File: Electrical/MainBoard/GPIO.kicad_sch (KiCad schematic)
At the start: 1 part, among them J17 GPIO

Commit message: Begin layout of pcb
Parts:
- renumbered J17 to J16
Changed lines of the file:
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@@
   (symbol (lib_id "Connector_Generic:Conn_02x10_Odd_Even") (at 149.86 94.615 0) (unit 1)
     (in_bom yes) (on_board yes) (dnp no) (fields_autoplaced)
-    (property "Reference" "J17" (at 151.13 78.74 0)
+    (property "Reference" "J16" (at 151.13 78.74 0)
       (effects (font (size 1.27 1.27)))
     )
@@
       (project "MainBoard"
         (path "/bd24c4db-4e36-4117-bd4f-5228ef241da9/7681952e-9ac4-4545-8f8a-d83e518f0640"
-          (reference "J17") (unit 1)
+          (reference "J16") (unit 1)
         )
       )

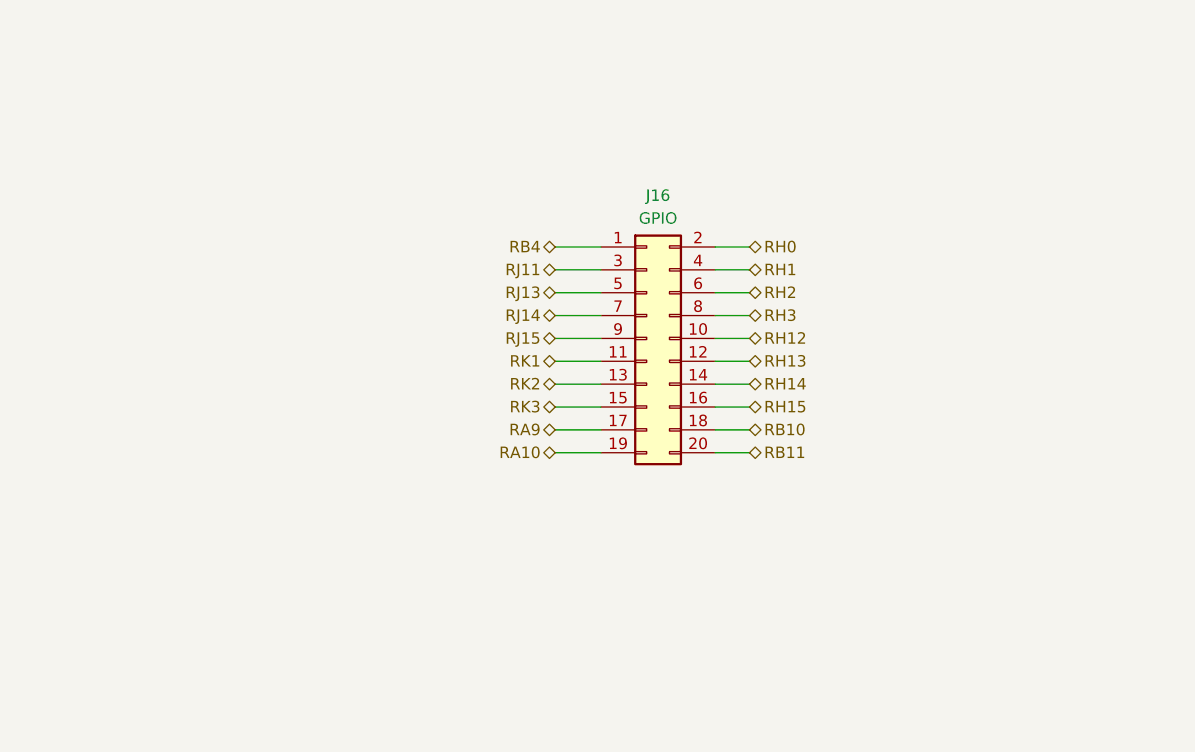
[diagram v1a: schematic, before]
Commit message: First Pass at the routing
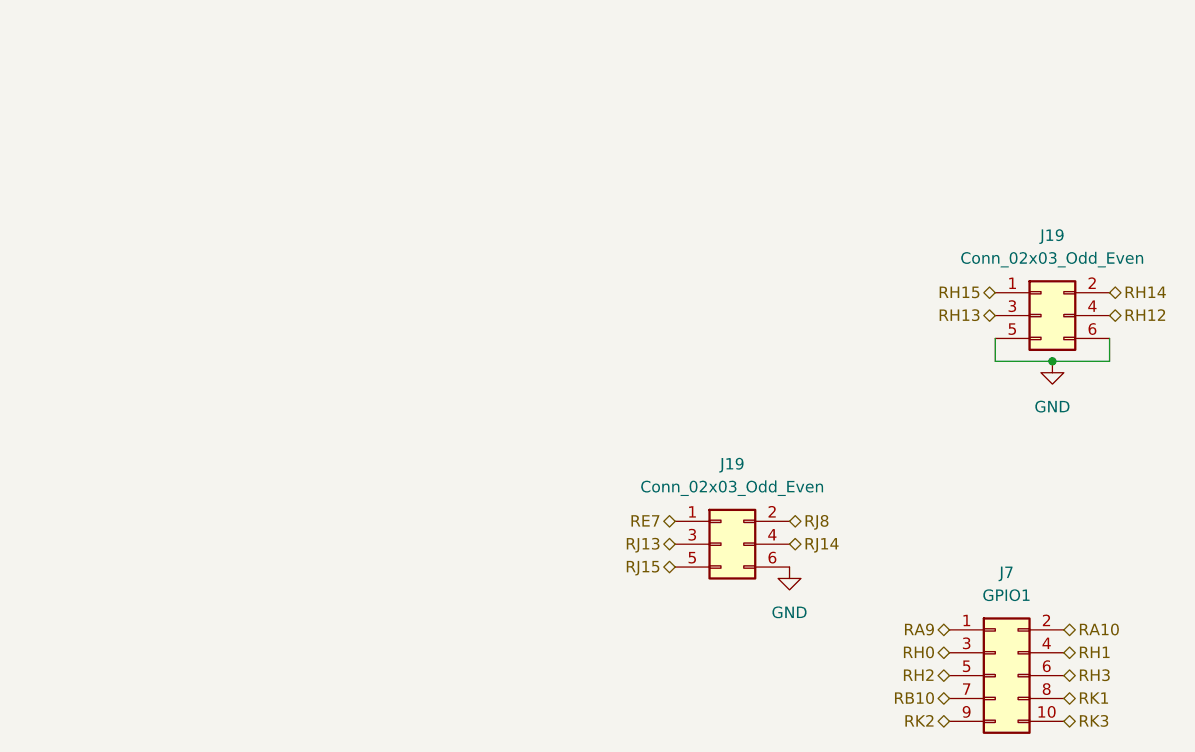
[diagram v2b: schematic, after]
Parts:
- removed J16: GPIO, Connector_PinHeader_2.54mm:PinHeader_2x10_P2.54mm_Vertical, symbol Connector_Generic:Conn_02x10_Odd_Even
- added J19 (x2): Conn_02x03_Odd_Even, Connector_PinHeader_2.54mm:PinHeader_2x03_P2.54mm_Vertical, symbol Connector_Generic:Conn_02x03_Odd_Even
- added J7: GPIO1, Connector_PinHeader_2.54mm:PinHeader_2x05_P2.54mm_Vertical, symbol Connector_Generic:Conn_02x05_Odd_Even
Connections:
- net RA10: now also J7.2 (Pin_2)
- net RA9: now also J7.1 (Pin_1)
- net RB10: now also J7.7 (Pin_7)
- net RH0: now also J7.3 (Pin_3)
- net RH1: now also J7.4 (Pin_4)
- net RH12: now also J19.4 (Pin_4)
- net RH13: now also J19.3 (Pin_3)
- net RH14: now also J19.2 (Pin_2)
- net RH15: now also J19.1 (Pin_1)
- net RH2: now also J7.5 (Pin_5)
- net RH3: now also J7.6 (Pin_6)
- net RJ13: now also J19.3 (Pin_3)
- net RJ14: now also J19.4 (Pin_4)
- net RJ15: now also J19.5 (Pin_5)
- net RK1: now also J7.8 (Pin_8)
- net RK2: now also J7.9 (Pin_9)
- net RK3: now also J7.10 (Pin_10)
- new net GND: J19.5 (Pin_5), J19.6 (Pin_6), J19.6 (Pin_6)
- new net RE7: J19.1 (Pin_1)
- new net RJ8: J19.2 (Pin_2)

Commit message: Add some finishing touches and create preliminary boms
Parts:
- J19: Mfr (none) -> Amphenol ICC (FCI); Mfr P/N (none) -> 10129381-906002BLF; Supplier 1 (none) -> DigiKey; Supplier 1 P/N (none) -> 10129381-906002BLF-ND
- J7: Mfr (none) -> Amphenol ICC (FCI); Mfr P/N (none) -> 10129381-910001BLF; Supplier 1 (none) -> DigiKey; Supplier 1 P/N (none) -> 10129381-910001BLF-ND
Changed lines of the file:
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@@
       (effects (font (size 1.27 1.27)) hide)
     )
-    (property "Datasheet" "~" (at 193.675 92.075 0)
+    (property "Datasheet" "https://cdn.amphenol-cs.com/media/wysiwyg/files/drawing/10129381.pdf" (at 193.675 92.075 0)
       (effects (font (size 1.27 1.27)) hide)
     )
-    (property "Description" "" (at 193.675 92.075 0)
+    (property "Description" "CONN HEADER VERT 6POS 2.54MM" (at 193.675 92.075 0)
       (effects (font (size 1.27 1.27)) hide)
     )
-    (property "Mfr" "" (at 193.675 92.075 0)
+    (property "Mfr" "Amphenol ICC (FCI)" (at 193.675 92.075 0)
       (effects (font (size 1.27 1.27)) hide)
     )
-    (property "Mfr P/N" "" (at 193.675 92.075 0)
+    (property "Mfr P/N" "10129381-906002BLF" (at 193.675 92.075 0)
       (effects (font (size 1.27 1.27)) hide)
     )
-    (property "Supplier 1" "" (at 193.675 92.075 0)
+    (property "Supplier 1" "DigiKey" (at 193.675 92.075 0)
       (effects (font (size 1.27 1.27)) hide)
     )
-    (property "Supplier 1 P/N" "" (at 193.675 92.075 0)
+    (property "Supplier 1 P/N" "10129381-906002BLF-ND" (at 193.675 92.075 0)
       (effects (font (size 1.27 1.27)) hide)
     )
@@
       (effects (font (size 1.27 1.27)) hide)
     )
-    (property "Datasheet" "~" (at 188.595 132.08 0)
+    (property "Datasheet" "https://cdn.amphenol-cs.com/media/wysiwyg/files/drawing/10129381.pdf" (at 188.595 132.08 0)
       (effects (font (size 1.27 1.27)) hide)
     )
-    (property "Description" "" (at 188.595 132.08 0)
+    (property "Description" "CONN HEADER VERT 10POS 2.54MM" (at 188.595 132.08 0)
       (effects (font (size 1.27 1.27)) hide)
     )
-    (property "Mfr" "" (at 188.595 132.08 0)
+    (property "Mfr" "Amphenol ICC (FCI)" (at 188.595 132.08 0)
       (effects (font (size 1.27 1.27)) hide)
     )
-    (property "Mfr P/N" "" (at 188.595 132.08 0)
+    (property "Mfr P/N" "10129381-910001BLF" (at 188.595 132.08 0)
       (effects (font (size 1.27 1.27)) hide)
     )
-    (property "Supplier 1" "" (at 188.595 132.08 0)
+    (property "Supplier 1" "DigiKey" (at 188.595 132.08 0)
       (effects (font (size 1.27 1.27)) hide)
     )
-    (property "Supplier 1 P/N" "" (at 188.595 132.08 0)
+    (property "Supplier 1 P/N" "10129381-910001BLF-ND" (at 188.595 132.08 0)
       (effects (font (size 1.27 1.27)) hide)
     )
@@
       (effects (font (size 1.27 1.27)) hide)
     )
-    (property "Datasheet" "~" (at 158.115 117.475 0)
+    (property "Datasheet" "https://cdn.amphenol-cs.com/media/wysiwyg/files/drawing/10129381.pdf" (at 158.115 117.475 0)
       (effects (font (size 1.27 1.27)) hide)
     )
-    (property "Description" "" (at 158.115 117.475 0)
+    (property "Description" "CONN HEADER VERT 6POS 2.54MM" (at 158.115 117.475 0)
       (effects (font (size 1.27 1.27)) hide)
     )
-    (property "Mfr" "" (at 158.115 117.475 0)
+    (property "Mfr" "Amphenol ICC (FCI)" (at 158.115 117.475 0)
       (effects (font (size 1.27 1.27)) hide)
     )
-    (property "Mfr P/N" "" (at 158.115 117.475 0)
+    (property "Mfr P/N" "10129381-906002BLF" (at 158.115 117.475 0)
       (effects (font (size 1.27 1.27)) hide)
     )
-    (property "Supplier 1" "" (at 158.115 117.475 0)
+    (property "Supplier 1" "DigiKey" (at 158.115 117.475 0)
       (effects (font (size 1.27 1.27)) hide)
     )
-    (property "Supplier 1 P/N" "" (at 158.115 117.475 0)
+    (property "Supplier 1 P/N" "10129381-906002BLF-ND" (at 158.115 117.475 0)
       (effects (font (size 1.27 1.27)) hide)
     )

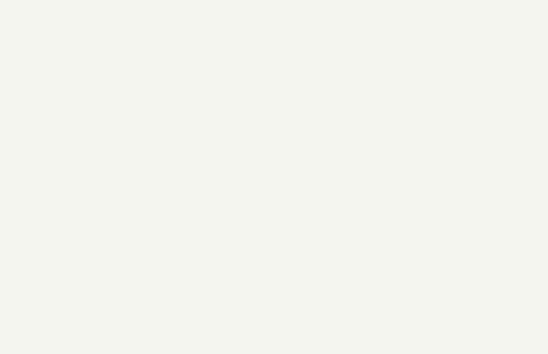
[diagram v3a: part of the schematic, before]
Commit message: Finish final board design for Rev 0.1 Main board and reflective Sensor. Created Gerbers.
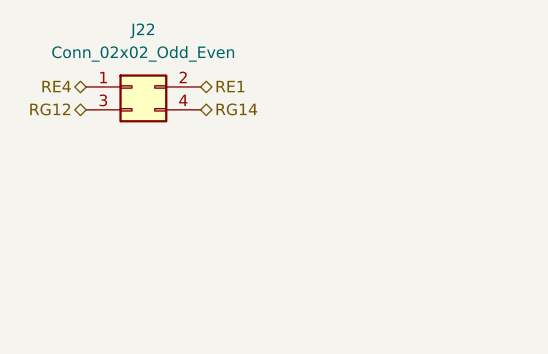
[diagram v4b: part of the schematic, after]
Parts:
- added J22: Conn_02x02_Odd_Even, Connector_PinHeader_2.54mm:PinHeader_2x02_P2.54mm_Vertical, symbol Connector_Generic:Conn_02x02_Odd_Even
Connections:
- new net RE1: J22.2 (Pin_2)
- new net RE4: J22.1 (Pin_1)
- new net RG12: J22.3 (Pin_3)
- new net RG14: J22.4 (Pin_4)
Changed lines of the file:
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@@
+    (effects (font (size 1.27 1.27)) (justify left))
+  )
+  (hierarchical_label "RE4" (shape bidirectional) (at 126.365 66.675 180) (fields_autoplaced)
+    (effects (font (size 1.27 1.27)) (justify right))
+  )
+  (hierarchical_label "RG14" (shape bidirectional) (at 139.065 69.215 0) (fields_autoplaced)
+    (effects (font (size 1.27 1.27)) (justify left))
+  )
+  (hierarchical_label "RE1" (shape bidirectional) (at 139.065 66.675 0) (fields_autoplaced)
     (effects (font (size 1.27 1.27)) (justify left))
   )
   (hierarchical_label "RB10" (shape bidirectional) (at 183.515 134.62 180) (fields_autoplaced)
+    (effects (font (size 1.27 1.27)) (justify right))
+  )
+  (hierarchical_label "RG12" (shape bidirectional) (at 126.365 69.215 180) (fields_autoplaced)
     (effects (font (size 1.27 1.27)) (justify right))
   )
@@
         )
       )
+    )
+  )
+  (symbol (lib_id "Connector_Generic:Conn_02x02_Odd_Even") (at 131.445 66.675 0) (unit 1)
+    (in_bom yes) (on_board yes) (dnp no) (fields_autoplaced)
+    (property "Reference" "J22" (at 132.715 60.325 0)
+      (effects (font (size 1.27 1.27)))
+    )
+    (property "Value" "Conn_02x02_Odd_Even" (at 132.715 62.865 0)
+      (effects (font (size 1.27 1.27)))
+    )
+    (property "Footprint" "Connector_PinHeader_2.54mm:PinHeader_2x02_P2.54mm_Vertical" (at 131.445 66.675 0)
+      (effects (font (size 1.27 1.27)) hide)
+    )
+    (property "Datasheet" "https://cdn.amphenol-cs.com/media/wysiwyg/files/drawing/10129381.pdf" (at 131.445 66.675 0)
+      (effects (font (size 1.27 1.27)) hide)
+    )
+    (property "Description" "CONN HEADER VERT 4POS 2.54MM" (at 131.445 66.675 0)
+      (effects (font (size 1.27 1.27)) hide)
+    )
+    (property "Mfr" "Amphenol ICC (FCI)" (at 131.445 66.675 0)
+      (effects (font (size 1.27 1.27)) hide)
+    )
+    (property "Mfr P/N" "10129381-904003BLF" (at 131.445 66.675 0)
+      (effects (font (size 1.27 1.27)) hide)
+    )
+    (property "Supplier 1" "DigiKey" (at 131.445 66.675 0)
+      (effects (font (size 1.27 1.27)) hide)
+    )
+    (property "Supplier 1 P/N" "10129381-904003BLF-ND" (at 131.445 66.675 0)
+      (effects (font (size 1.27 1.27)) hide)
+    )
+    (property "Supplier 2" "" (at 131.445 66.675 0)
+      (effects (font (size 1.27 1.27)) hide)
+    )
+    (property "Supplier 2 P/N" "" (at 131.445 66.675 0)
+      (effects (font (size 1.27 1.27)) hide)
+    )
+    (pin "1")
+    (pin "2")
+    (pin "3")
+    (pin "4")
+    (instances
+      (project "MainBoard"
+        (path "/bd24c4db-4e36-4117-bd4f-5228ef241da9/d895d168-5c3b-4f65-b0f2-4d47b39f1a08"
+          (reference "J22") (unit 1)
+        )
+        (path "/bd24c4db-4e36-4117-bd4f-5228ef241da9/7681952e-9ac4-4545-8f8a-d83e518f0640"
+          (reference "J25") (unit 1)
+        )
+      )

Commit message: Made V0.2 revisions to Main Board
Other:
- company: (none) -> satomm@stanford.edu
- title: (none) -> MCU Controller
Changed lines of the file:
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@@
 (kicad_sch (version 20230121) (generator eeschema)
   (paper "A4")
+  (title_block
+    (title "MCU Controller")
+    (rev "0.2")
+    (company "satomm@stanford.edu")
+    (comment 1 "Department of Civil and Environmental Engineering")
+    (comment 2 "Engineering Informatics Group")
+    (comment 3 "Stanford University")
+    (comment 4 "Matthew Sato")
+  )
   (junction (at 194.945 97.155) (diameter 0) (color 0 0 0 0)
   )

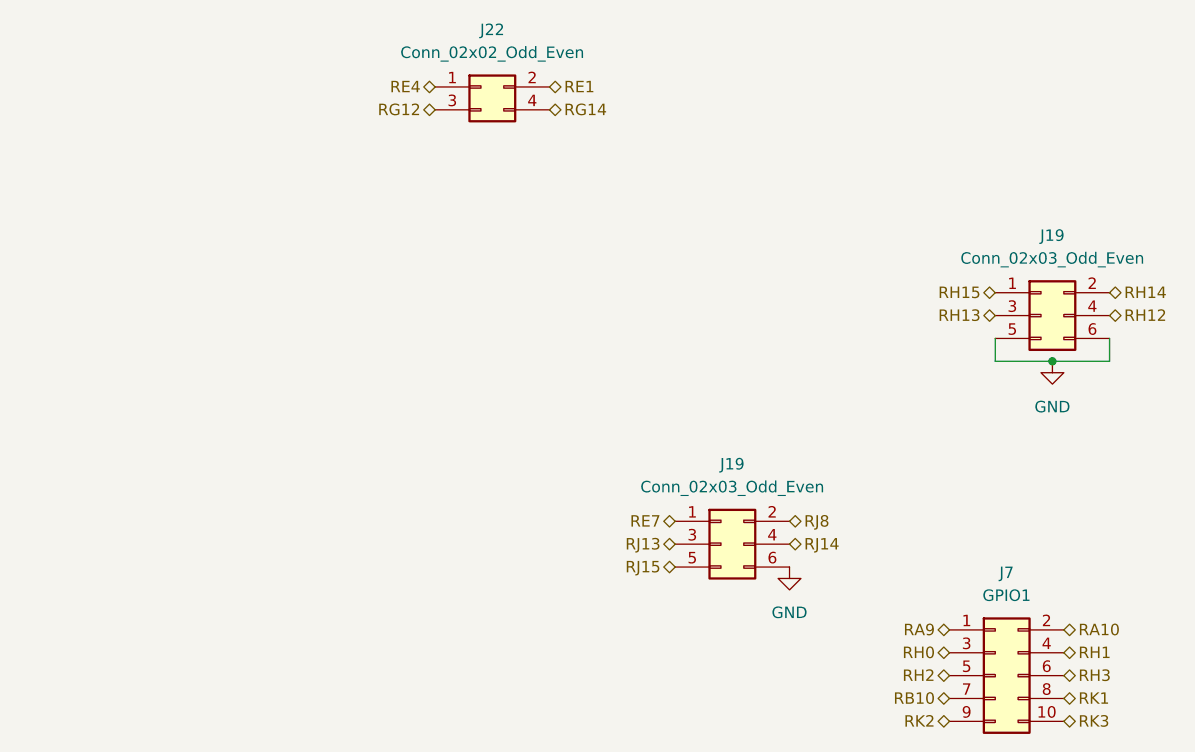
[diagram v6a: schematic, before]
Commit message: Fix SPI3 and make visual improvements
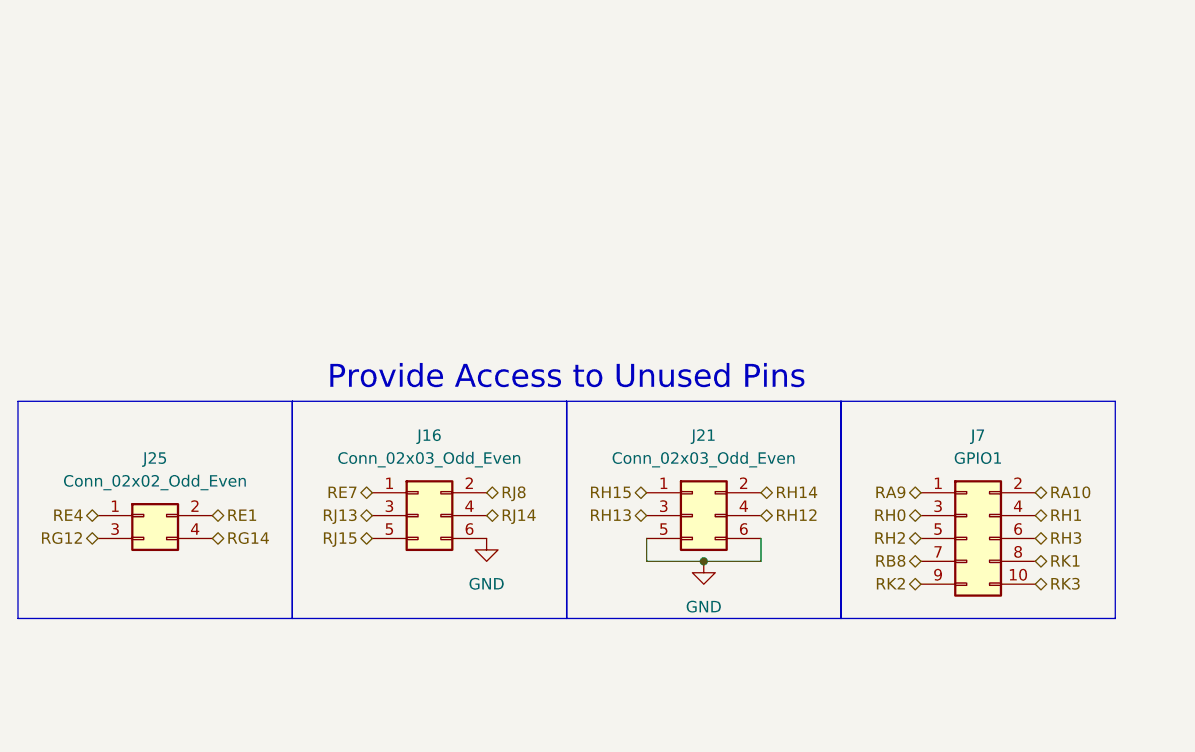
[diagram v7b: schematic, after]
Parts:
- renumbered J19 to J16, J19 to J21, J22 to J25
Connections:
- net RB10 renamed RB8
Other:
- note added: "Provide Access to Unused Pins"
- moved on the sheet: J16, J21, J25, J7

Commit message: Update some parts
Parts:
- J16, J21, J25, J7: now left out of the parts list
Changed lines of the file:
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@@
 		(unit 1)
 		(exclude_from_sim no)
-		(in_bom yes)
+		(in_bom no)
 		(on_board yes)
 		(dnp no)
@@
 		(unit 1)
 		(exclude_from_sim no)
-		(in_bom yes)
+		(in_bom no)
 		(on_board yes)
 		(dnp no)
@@
 		(unit 1)
 		(exclude_from_sim no)
-		(in_bom yes)
+		(in_bom no)
 		(on_board yes)
 		(dnp no)
@@
 		(unit 1)
 		(exclude_from_sim no)
-		(in_bom yes)
+		(in_bom no)
 		(on_board yes)
 		(dnp no)
